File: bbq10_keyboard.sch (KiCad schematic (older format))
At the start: 17 parts, among them J1 PMOD, Q1 BSS138, U1 BBQ10KBD, U2 ATSAMD20E16A

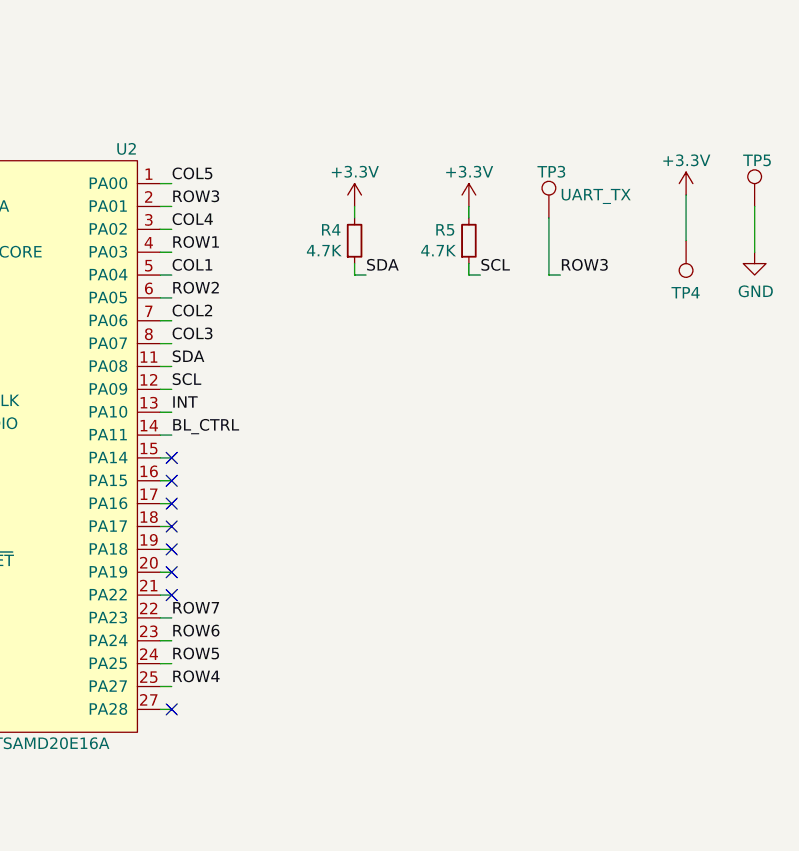
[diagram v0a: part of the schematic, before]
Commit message: rev2
- Made the right keyboard hole larger
- Moved the conenctor to the back
- Rerouted everything
- Fixed the damn 0201 footprints
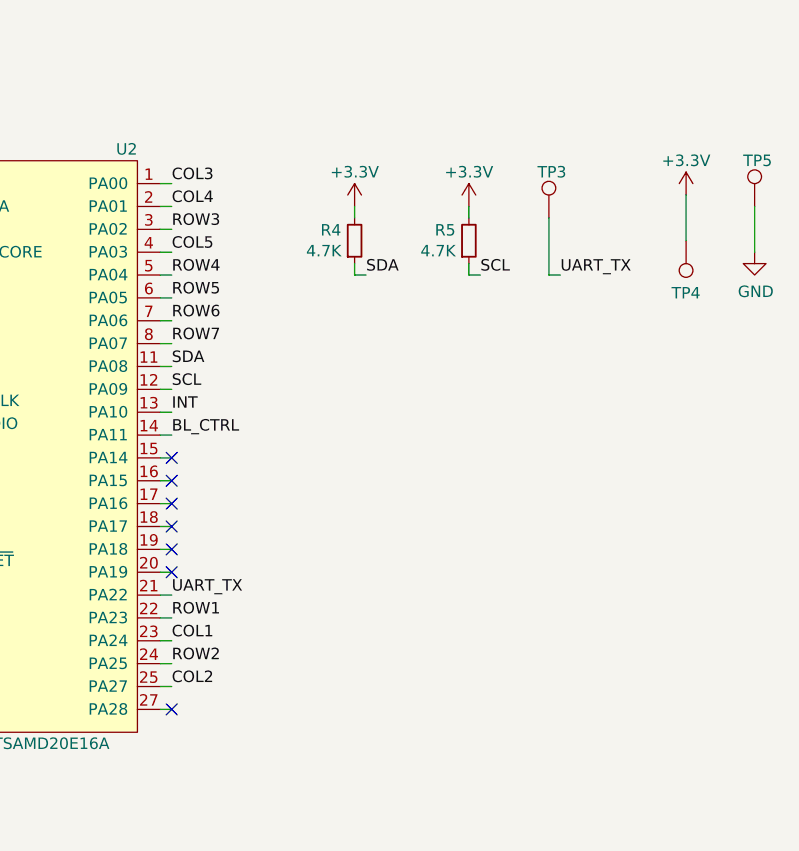
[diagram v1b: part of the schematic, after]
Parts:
- C1, C2, C3: footprint Capacitor_SMD:C_0201_0603Metric -> Capacitor_SMD:C_0603_1608Metric
- R1, R2, R3, R4, R5: footprint Resistor_SMD:R_0201_0603Metric -> Resistor_SMD:R_0603_1608Metric
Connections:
- net COL1: now also U2.23 (PA24); no longer U2.5 (PA04)
- net COL2: now also U2.25 (PA27); no longer U2.7 (PA06)
- net COL3: now also U2.1 (PA00); no longer U2.8 (PA07)
- net COL4: now also U2.2 (PA01); no longer U2.3 (PA02)
- net COL5: now also U2.4 (PA03); no longer U2.1 (PA00)
- net ROW1: now also U2.22 (PA23); no longer U2.4 (PA03)
- net ROW2: now also U2.24 (PA25); no longer U2.6 (PA05)
- net ROW3: now also U2.3 (PA02); no longer TP3.1, U2.2 (PA01)
- net ROW4: now also U2.5 (PA04); no longer U2.25 (PA27)
- net ROW5: now also U2.6 (PA05); no longer U2.24 (PA25)
- net ROW6: now also U2.7 (PA06); no longer U2.23 (PA24)
- net ROW7: now also U2.8 (PA07); no longer U2.22 (PA23)
- net UART_TX: now reaches U2.21 (PA22)
- net UART_TX: now also TP3.1
- no-connect marks 11 -> 10
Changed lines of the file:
@@
 F 0 "C1" V 6400 2850 50  0000 R CNN
 F 1 "0.1uF" V 6400 2950 50  0000 L CNN
-F 2 "Capacitor_SMD:C_0201_0603Metric" H 6450 2900 50  0001 C CNN
+F 2 "Capacitor_SMD:C_0603_1608Metric" H 6450 2900 50  0001 C CNN
 F 3 "~" H 6450 2900 50  0001 C CNN
 	1    6450 2900
@@
 F 0 "C2" V 6400 2950 50  0000 R CNN
 F 1 "4.7uF" V 6400 3050 50  0000 L CNN
-F 2 "Capacitor_SMD:C_0201_0603Metric" H 6450 3000 50  0001 C CNN
+F 2 "Capacitor_SMD:C_0603_1608Metric" H 6450 3000 50  0001 C CNN
 F 3 "~" H 6450 3000 50  0001 C CNN
 	1    6450 3000
@@
 F 0 "C3" V 6400 3150 50  0000 R CNN
 F 1 "1uF" V 6400 3250 50  0000 L CNN
-F 2 "Capacitor_SMD:C_0201_0603Metric" H 6450 3200 50  0001 C CNN
+F 2 "Capacitor_SMD:C_0603_1608Metric" H 6450 3200 50  0001 C CNN
 F 3 "~" H 6450 3200 50  0001 C CNN
 	1    6450 3200
@@
 F 0 "R2" H 6641 3654 50  0000 R CNN
 F 1 "1K" H 6641 3745 50  0000 R CNN
-F 2 "Resistor_SMD:R_0201_0603Metric" H 6700 3700 50  0001 C CNN
+F 2 "Resistor_SMD:R_0603_1608Metric" H 6700 3700 50  0001 C CNN
 F 3 "~" H 6700 3700 50  0001 C CNN
 	1    6700 3700
@@
 Text Label 7850 4000 0    50   ~ 0
 BL_CTRL
+Text Label 7850 4800 0    50   ~ 0
+ROW1
+Text Label 7850 4900 0    50   ~ 0
+COL1
+Text Label 7850 5000 0    50   ~ 0
+ROW2
+Text Label 7850 5100 0    50   ~ 0
+COL2
+Text Label 7850 2900 0    50   ~ 0
+COL3
+Text Label 7850 3000 0    50   ~ 0
+COL4
+Text Label 7850 3100 0    50   ~ 0
+ROW3
 Text Label 7850 3200 0    50   ~ 0
-ROW1
+COL5
 Text Label 7850 3300 0    50   ~ 0
-COL1
+ROW4
 Text Label 7850 3400 0    50   ~ 0
-ROW2
+ROW5
 Text Label 7850 3500 0    50   ~ 0
-COL2
+ROW6
 Text Label 7850 3600 0    50   ~ 0
-COL3
-Text Label 7850 3100 0    50   ~ 0
-COL4
-Text Label 7850 3000 0    50   ~ 0
-ROW3
-Text Label 7850 2900 0    50   ~ 0
-COL5
-Text Label 7850 5100 0    50   ~ 0
-ROW4
-Text Label 7850 5000 0    50   ~ 0
-ROW5
-Text Label 7850 4900 0    50   ~ 0
-ROW6
-Text Label 7850 4800 0    50   ~ 0
 ROW7
 $Comp
@@
 F 0 "R4" H 8592 3104 50  0000 R CNN
 F 1 "4.7K" H 8592 3195 50  0000 R CNN
-F 2 "Resistor_SMD:R_0201_0603Metric" H 8650 3150 50  0001 C CNN
+F 2 "Resistor_SMD:R_0603_1608Metric" H 8650 3150 50  0001 C CNN
 F 3 "~" H 8650 3150 50  0001 C CNN
 	1    8650 3150
@@
 F 0 "R5" H 9092 3104 50  0000 R CNN
 F 1 "4.7K" H 9092 3195 50  0000 R CNN
-F 2 "Resistor_SMD:R_0201_0603Metric" H 9150 3150 50  0001 C CNN
+F 2 "Resistor_SMD:R_0603_1608Metric" H 9150 3150 50  0001 C CNN
 F 3 "~" H 9150 3150 50  0001 C CNN
 	1    9150 3150
@@
 $EndComp
 Text Label 9550 3300 0    50   ~ 0
-ROW3
+UART_TX
 $Comp
 L Connector:TestPoint TP3
@@
 P 9500 3050
 F 0 "TP3" H 9450 3250 50  0000 L CNN
-F 1 "UART_TX" H 9550 3150 50  0000 L CNN
+F 1 "UART_TX" H 9550 3150 50  0001 L CNN
 F 2 "TestPoint:TestPoint_Pad_D1.0mm" H 9700 3050 50  0001 C CNN
 F 3 "~" H 9700 3050 50  0001 C CNN
@@
 F 0 "R1" H 2292 4154 50  0000 R CNN
 F 1 "10K" H 2292 4245 50  0000 R CNN
-F 2 "Resistor_SMD:R_0201_0603Metric" H 2350 4200 50  0001 C CNN
+F 2 "Resistor_SMD:R_0603_1608Metric" H 2350 4200 50  0001 C CNN
 F 3 "~" H 2350 4200 50  0001 C CNN
 	1    2350 4200
@@
 F 0 "R3" H 6642 4354 50  0000 R CNN
 F 1 "10K" H 6642 4445 50  0000 R CNN
-F 2 "Resistor_SMD:R_0201_0603Metric" H 6700 4400 50  0001 C CNN
+F 2 "Resistor_SMD:R_0603_1608Metric" H 6700 4400 50  0001 C CNN
 F 3 "~" H 6700 4400 50  0001 C CNN
 	1    6700 4400
@@
 Wire Wire Line
 	7800 3600 7850 3600
-NoConn ~ 7850 4100
-NoConn ~ 7850 4200
-NoConn ~ 7850 4300
-NoConn ~ 7850 4400
-NoConn ~ 7850 4500
-NoConn ~ 7850 4600
-NoConn ~ 7850 4700
 $Comp
 L power:+3.3V #PWR0101
@@
 Wire Wire Line
 	10400 3000 10400 3200
+Text Label 7850 4700 0    50   ~ 0
+UART_TX
+NoConn ~ 7850 4100
+NoConn ~ 7850 4200
+NoConn ~ 7850 4300
+NoConn ~ 7850 4400
+NoConn ~ 7850 4500
+NoConn ~ 7850 4600
 NoConn ~ 7850 5200
 $EndSCHEMATC
